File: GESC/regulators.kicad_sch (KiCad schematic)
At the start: 16 parts, among them J7 Conn_01x02, U1 PQDE6W-Q110 / RD5-110S12W, U2 TO220_replacement_module, U3 LM1117DT-3.3

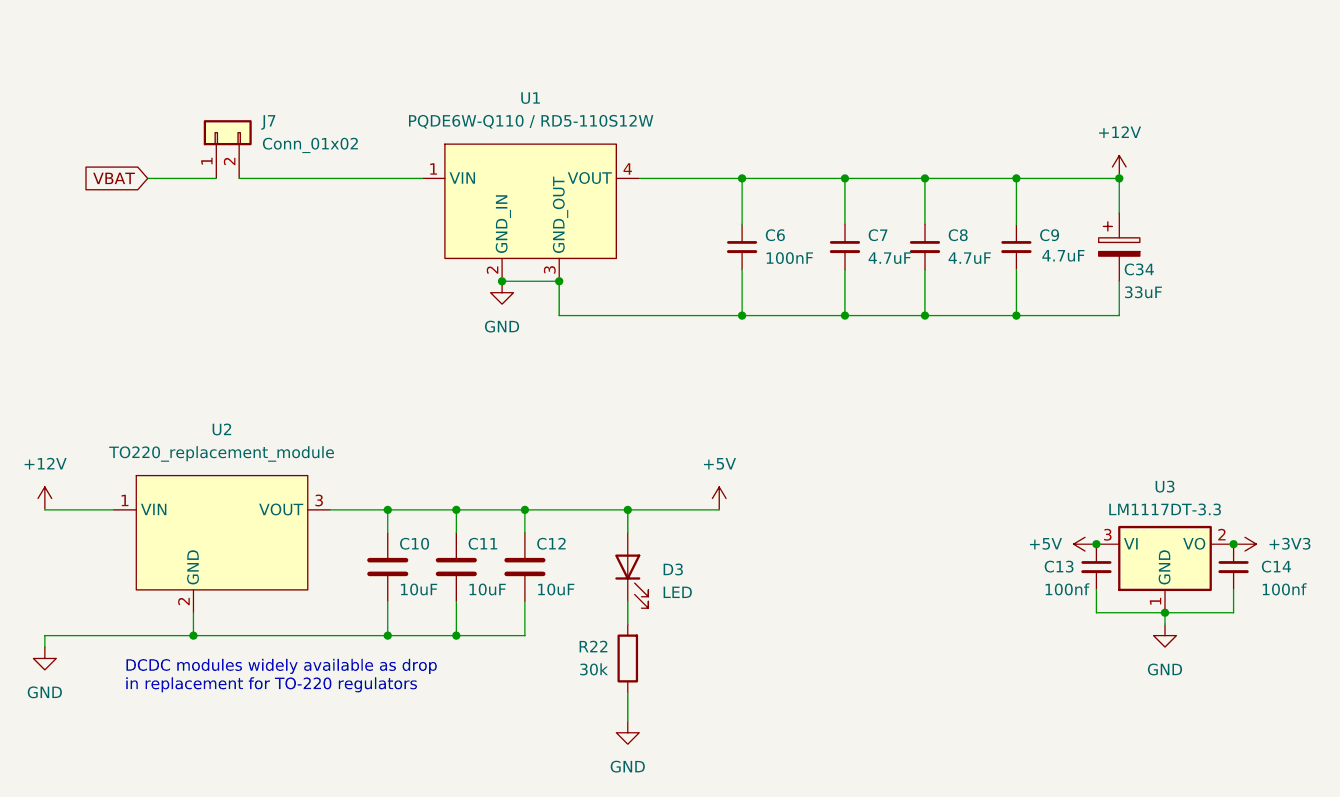
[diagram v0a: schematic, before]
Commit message: full to power board only
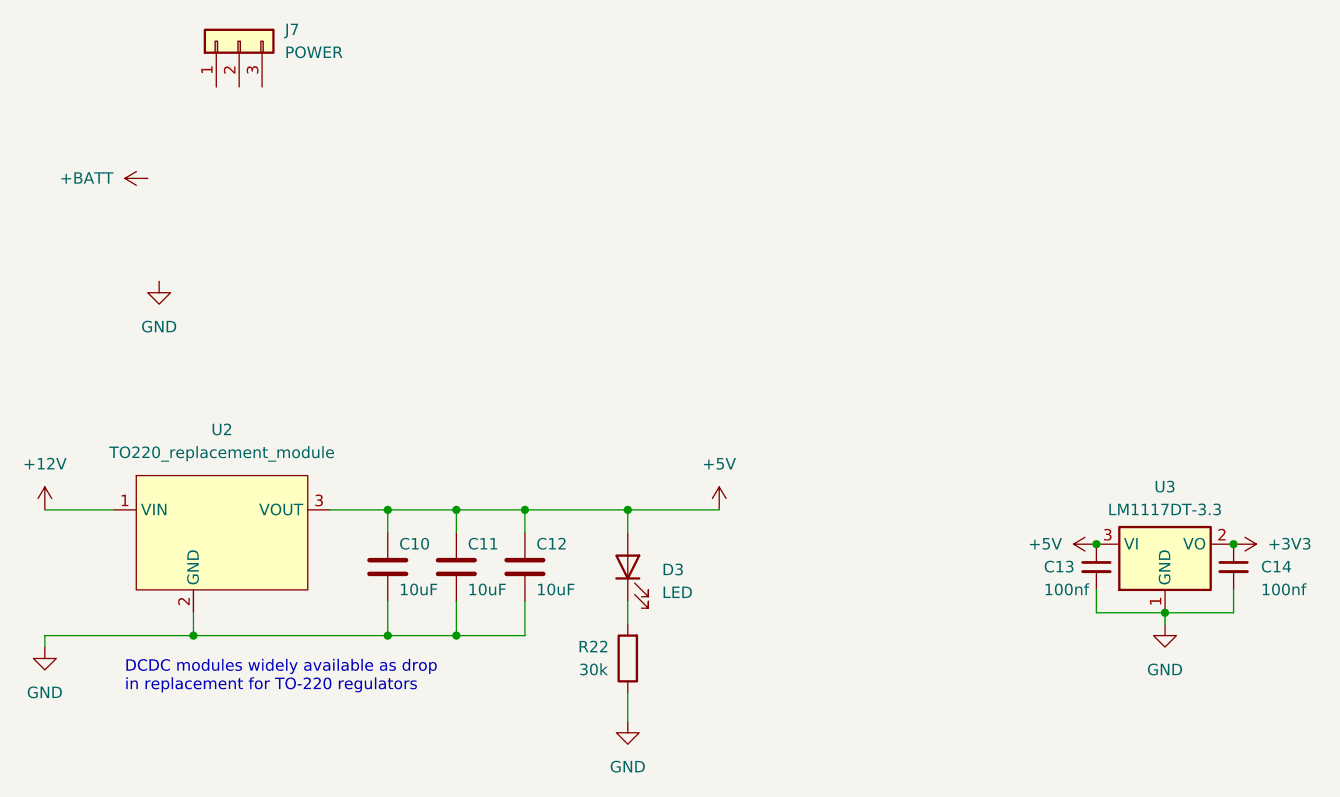
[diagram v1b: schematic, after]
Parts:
- removed C34: 33uF, symbol Device:C_Polarized
- removed C6: 100nF, Capacitor_SMD:C_0603_1608Metric, symbol Device:C_Small
- removed C7, C8, C9: 4.7uF, Capacitor_SMD:C_0603_1608Metric, symbol Device:C_Small
- removed J7: Conn_01x02, symbol Connector_Generic:Conn_01x02
- removed U1: PQDE6W-Q110 / RD5-110S12W, CCC_ESC_Custom_parts:PQDE6W, symbol CCC_ESC_Custom_Symbols:PQDE6W-Q110
- added J7: POWER, Connector_JST:JST_GH_BM03B-GHS-TBT_1x03-1MP_P1.25mm_Vertical, symbol Connector_Generic:Conn_01x03
- C13: footprint Capacitor_Tantalum_SMD:CP_EIA-3216-18_Kemet-A -> Capacitor_SMD:C_0603_1608Metric
